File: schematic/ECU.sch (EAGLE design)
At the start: 29 parts, among them J1 Break, J2 COMM, J3 PWR, J4 DISPLAY, J5 THROTTLE, J6 LED, J7 SPEED, Q1 NMOSFETSOT23, Q2 NMOSFETSOT23, Q4 PMOSFET_BSS84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

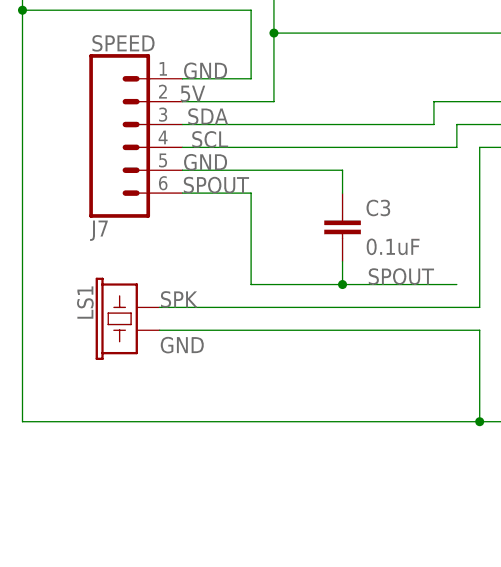
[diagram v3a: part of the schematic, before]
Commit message: Replace buzzer with 7.6mm contacts spacing
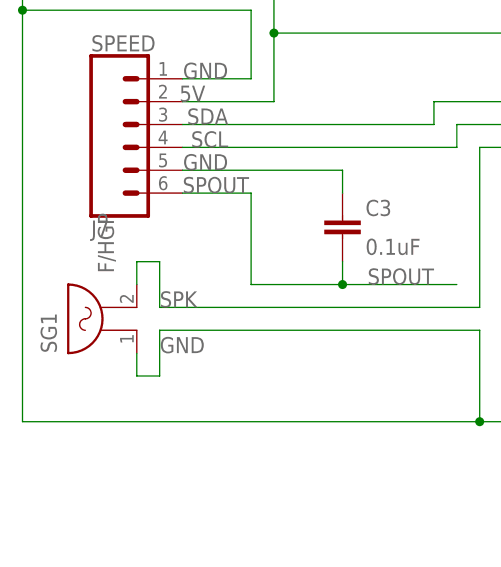
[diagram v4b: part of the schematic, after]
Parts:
- removed LS1: BUZZER-PTH_KIT, SparkFun-Electromechanical:BUZZER-PTH_KIT
- added SG1: F/HGP, buzzer:F/HGP
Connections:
- net GND: now also SG1.1; no longer LS1.2
- net SPK: now also SG1.2; no longer LS1.1
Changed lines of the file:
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@@
 <part name="C3" library="Capacitor" library_urn="urn:adsk.eagle:library:16290819" deviceset="C" device="CHIP-1206(3216-METRIC)" package3d_urn="urn:adsk.eagle:package:16290893/2" technology="_" value="0.1uF"/>
 <part name="Q1" library="Transistor" library_urn="urn:adsk.eagle:library:16378713" deviceset="NMOSFET" device="SOT23" package3d_urn="urn:adsk.eagle:package:28738/2"/>
-<part name="LS1" library="SparkFun-Electromechanical" library_urn="urn:adsk.eagle:library:516" deviceset="BUZZER" device="-PTH_KIT" package3d_urn="urn:adsk.eagle:package:38556/1"/>
 <part name="R3" library="eagle-ltspice" library_urn="urn:adsk.eagle:library:217" deviceset="R" device="R1206" package3d_urn="urn:adsk.eagle:package:13301/1" value="10K"/>
 <part name="D4" library="eScooter" deviceset="TVS_DIODE" device="SMA" package3d_urn="urn:adsk.eagle:package:21928182/1"/>
@@
 <part name="GND2" library="supply1" library_urn="urn:adsk.eagle:library:371" deviceset="GND" device=""/>
 <part name="U1" library="eScooter" deviceset="ARDUINO" device="ARDUINO_NANO" package3d_urn="urn:adsk.eagle:package:21849926/1" value="Arduino Nano Every"/>
+<part name="SG1" library="buzzer" library_urn="urn:adsk.eagle:library:113" deviceset="F/HGP" device="" package3d_urn="urn:adsk.eagle:package:5287/1"/>
 </parts>
 <sheets>
@@
 <attribute name="NAME" x="128.27" y="85.09" size="1.778" layer="95"/>
 </instance>
-<instance part="LS1" gate="G$1" x="-66.04" y="40.64" smashed="yes" rot="MR270">
-<attribute name="NAME" x="-70.866" y="43.18" size="1.778" layer="95" font="vector" rot="MR270"/>
-</instance>
 <instance part="R3" gate="G$1" x="134.62" y="33.02" smashed="yes" rot="R90">
 <attribute name="NAME" x="133.1214" y="29.21" size="1.778" layer="95" rot="R90"/>
@@
 <attribute name="NAME" x="27.94" y="86.36" size="1.778" layer="95"/>
 <attribute name="VALUE" x="20.32" y="40.64" size="1.778" layer="96"/>
+</instance>
+<instance part="SG1" gate="G$1" x="-68.58" y="38.1" smashed="yes" rot="R90">
+<attribute name="NAME" x="-74.93" y="35.56" size="1.778" layer="95" rot="R90"/>
+<attribute name="VALUE" x="-68.58" y="44.45" size="1.778" layer="96" rot="R90"/>
 </instance>
 </instances>
@@
 <label x="10.16" y="48.26" size="1.778" layer="95"/>
 <wire x1="0" y1="48.26" x2="0" y2="27.94" width="0.1524" layer="91"/>
-<pinref part="LS1" gate="G$1" pin="2"/>
 <wire x1="-63.5" y1="38.1" x2="-27.94" y2="38.1" width="0.1524" layer="91"/>
 <wire x1="-27.94" y1="38.1" x2="-27.94" y2="27.94" width="0.1524" layer="91"/>
@@
 <wire x1="66.04" y1="-17.78" x2="73.66" y2="-17.78" width="0.1524" layer="91"/>
 <pinref part="U1" gate="G$1" pin="GND"/>
+<pinref part="SG1" gate="G$1" pin="1"/>
+<wire x1="-66.04" y1="35.56" x2="-66.04" y2="33.02" width="0.1524" layer="91"/>
+<wire x1="-66.04" y1="33.02" x2="-63.5" y2="33.02" width="0.1524" layer="91"/>
+<wire x1="-63.5" y1="33.02" x2="-63.5" y2="38.1" width="0.1524" layer="91"/>
 </segment>
 <segment>
@@
 <wire x1="-27.94" y1="58.42" x2="-27.94" y2="40.64" width="0.1524" layer="91"/>
 <label x="10.16" y="58.42" size="1.778" layer="95"/>
-<pinref part="LS1" gate="G$1" pin="1"/>
 <wire x1="-63.5" y1="40.64" x2="-27.94" y2="40.64" width="0.1524" layer="91"/>
 <label x="-63.5" y="40.64" size="1.778" layer="95"/>
 <pinref part="U1" gate="G$1" pin="A6"/>
-</segment>
-</net>
+<pinref part="SG1" gate="G$1" pin="2"/>
+<wire x1="-66.04" y1="43.18" x2="-66.04" y2="45.72" width="0.1524" layer="91"/>
+<wire x1="-66.04" y1="45.72" x2="-63.5" y2="45.72" width="0.1524" layer="91"/>
+<wire x1="-63.5" y1="45.72" x2="-63.5" y2="40.64" width="0.1524" layer="91"/>
+</segment>
+</net>

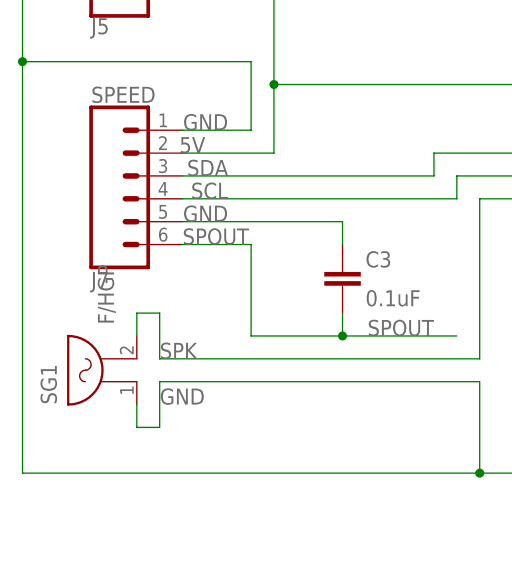
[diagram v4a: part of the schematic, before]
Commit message: Change MAX regulator package
- Change MAX package to drill-pin
- Move button to bottom layout
- Move elements for better work on regulator and ECU
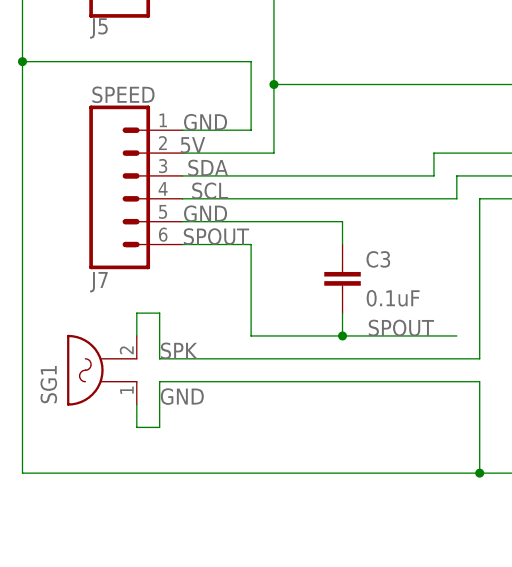
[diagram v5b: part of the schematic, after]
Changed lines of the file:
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@@
 <part name="Q4" library="Transistor" library_urn="urn:adsk.eagle:library:16378713" deviceset="PMOSFET_" device="" package3d_urn="urn:adsk.eagle:package:28738/2" technology="BSS84" value=""/>
 <part name="D3" library="Diode" library_urn="urn:adsk.eagle:library:16378169" deviceset="DIODE" device="DO-215-AC" package3d_urn="urn:adsk.eagle:package:9427057/2" technology="_" value=""/>
-<part name="S1" library="SparkFun-Switches" library_urn="urn:adsk.eagle:library:535" deviceset="MOMENTARY-SWITCH-SPST" device="-PTH-6.0MM" package3d_urn="urn:adsk.eagle:package:40163/1" value=""/>
 <part name="Q5" library="Transistor" library_urn="urn:adsk.eagle:library:16378713" deviceset="NMOSFET" device="SOT23" package3d_urn="urn:adsk.eagle:package:28738/2"/>
 <part name="J7" library="SparkFun-Connectors" library_urn="urn:adsk.eagle:library:513" deviceset="CONN_06" device="SILK_FEMALE_PTH" package3d_urn="urn:adsk.eagle:package:38009/1" value="SPEED"/>
@@
 <part name="GND2" library="supply1" library_urn="urn:adsk.eagle:library:371" deviceset="GND" device=""/>
 <part name="U1" library="eScooter" deviceset="ARDUINO" device="ARDUINO_NANO" package3d_urn="urn:adsk.eagle:package:21849926/1" value="Arduino Nano Every"/>
-<part name="SG1" library="buzzer" library_urn="urn:adsk.eagle:library:113" deviceset="F/HGP" device="" package3d_urn="urn:adsk.eagle:package:5287/1"/>
+<part name="S1" library="SparkFun-Switches" deviceset="MOMENTARY-SWITCH-SPST" device="-PTH-6.0MM" package3d_urn="urn:adsk.eagle:package:40163/1"/>
+<part name="SG1" library="buzzer" deviceset="F/HGP" device="" package3d_urn="urn:adsk.eagle:package:5287/1"/>
 </parts>
 <sheets>
@@
 <attribute name="VALUE" x="81.28" y="-33.02" size="1.778" layer="95" align="center"/>
 </instance>
-<instance part="S1" gate="G$1" x="88.9" y="-10.16" smashed="yes">
-<attribute name="NAME" x="88.9" y="-8.636" size="1.778" layer="95" font="vector" align="bottom-center"/>
-<attribute name="VALUE" x="88.9" y="-10.668" size="1.778" layer="96" font="vector" align="top-center"/>
-</instance>
 <instance part="Q5" gate="G$1" x="88.9" y="50.8" smashed="yes" rot="MR0">
 <attribute name="NAME" x="82.55" y="52.07" size="1.778" layer="95" rot="MR0"/>
@@
 <attribute name="VALUE" x="20.32" y="40.64" size="1.778" layer="96"/>
 </instance>
+<instance part="S1" gate="G$1" x="88.9" y="-10.16" smashed="yes">
+<attribute name="NAME" x="88.9" y="-8.636" size="1.778" layer="95" font="vector" align="bottom-center"/>
+</instance>
 <instance part="SG1" gate="G$1" x="-68.58" y="38.1" smashed="yes" rot="R90">
 <attribute name="NAME" x="-74.93" y="35.56" size="1.778" layer="95" rot="R90"/>
-<attribute name="VALUE" x="-68.58" y="44.45" size="1.778" layer="96" rot="R90"/>
 </instance>
 </instances>
@@
 <wire x1="88.9" y1="-5.08" x2="88.9" y2="0" width="0.1524" layer="91"/>
 <label x="55.88" y="-10.16" size="1.778" layer="95"/>
-<pinref part="S1" gate="G$1" pin="1"/>
 <wire x1="88.9" y1="0" x2="88.9" y2="2.54" width="0.1524" layer="91"/>
 <wire x1="83.82" y1="-10.16" x2="76.2" y2="-10.16" width="0.1524" layer="91"/>
@@
 <wire x1="66.04" y1="-17.78" x2="73.66" y2="-17.78" width="0.1524" layer="91"/>
 <pinref part="U1" gate="G$1" pin="GND"/>
-<pinref part="SG1" gate="G$1" pin="1"/>
 <wire x1="-66.04" y1="35.56" x2="-66.04" y2="33.02" width="0.1524" layer="91"/>
 <wire x1="-66.04" y1="33.02" x2="-63.5" y2="33.02" width="0.1524" layer="91"/>
 <wire x1="-63.5" y1="33.02" x2="-63.5" y2="38.1" width="0.1524" layer="91"/>
+<pinref part="S1" gate="G$1" pin="1"/>
+<pinref part="SG1" gate="G$1" pin="1"/>
 </segment>
 <segment>
@@
 <wire x1="86.36" y1="-27.94" x2="99.06" y2="-27.94" width="0.1524" layer="91"/>
 <wire x1="99.06" y1="-10.16" x2="99.06" y2="-7.62" width="0.1524" layer="91"/>
-<pinref part="S1" gate="G$1" pin="2"/>
 <wire x1="99.06" y1="-17.78" x2="99.06" y2="-27.94" width="0.1524" layer="91"/>
 <wire x1="99.06" y1="-17.78" x2="88.9" y2="-17.78" width="0.1524" layer="91"/>
@@
 <wire x1="99.06" y1="-10.16" x2="99.06" y2="-17.78" width="0.1524" layer="91"/>
 <junction x="99.06" y="-10.16"/>
+<pinref part="S1" gate="G$1" pin="2"/>
 </segment>
 </net>
@@
 <label x="-63.5" y="40.64" size="1.778" layer="95"/>
 <pinref part="U1" gate="G$1" pin="A6"/>
-<pinref part="SG1" gate="G$1" pin="2"/>
 <wire x1="-66.04" y1="43.18" x2="-66.04" y2="45.72" width="0.1524" layer="91"/>
 <wire x1="-66.04" y1="45.72" x2="-63.5" y2="45.72" width="0.1524" layer="91"/>
 <wire x1="-63.5" y1="45.72" x2="-63.5" y2="40.64" width="0.1524" layer="91"/>
-</segment>
-</net>
+<pinref part="SG1" gate="G$1" pin="2"/>
+</segment>
+</net>

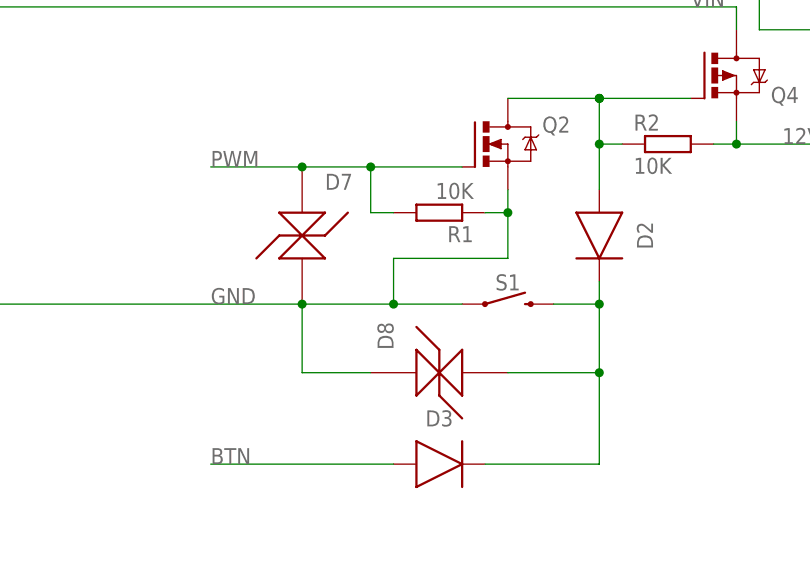
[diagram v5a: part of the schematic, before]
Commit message: Rework ECU board
- Align sizes
- Align elements placement on layers
- Change power traces in regulator
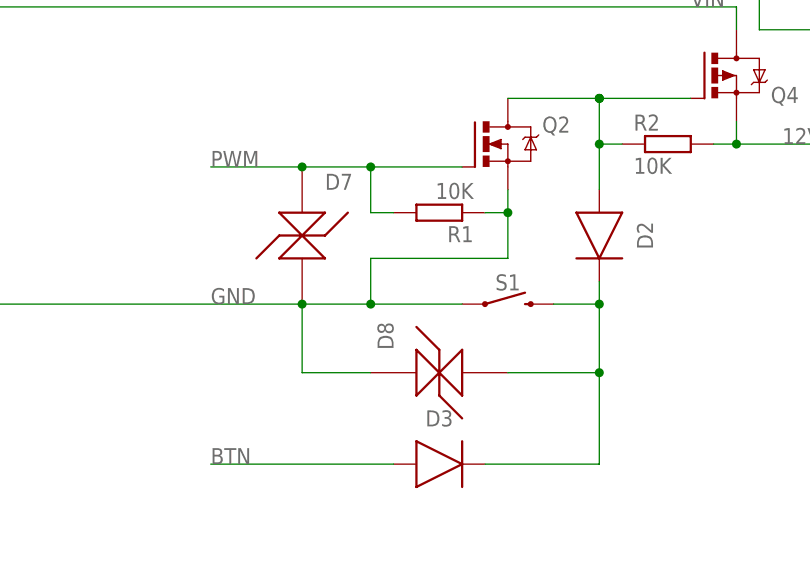
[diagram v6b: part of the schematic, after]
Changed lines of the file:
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@@
 <pinref part="R1" gate="G$1" pin="1"/>
 <pinref part="Q2" gate="G$1" pin="S"/>
-<wire x1="76.2" y1="-5.08" x2="88.9" y2="-5.08" width="0.1524" layer="91"/>
+<wire x1="73.66" y1="-5.08" x2="88.9" y2="-5.08" width="0.1524" layer="91"/>
 <wire x1="88.9" y1="-5.08" x2="88.9" y2="0" width="0.1524" layer="91"/>
 <label x="55.88" y="-10.16" size="1.778" layer="95"/>
 <wire x1="88.9" y1="0" x2="88.9" y2="2.54" width="0.1524" layer="91"/>
-<wire x1="83.82" y1="-10.16" x2="76.2" y2="-10.16" width="0.1524" layer="91"/>
-<wire x1="76.2" y1="-5.08" x2="76.2" y2="-10.16" width="0.1524" layer="91"/>
-<junction x="76.2" y="-10.16"/>
-<wire x1="76.2" y1="-10.16" x2="66.04" y2="-10.16" width="0.1524" layer="91"/>
+<wire x1="83.82" y1="-10.16" x2="73.66" y2="-10.16" width="0.1524" layer="91"/>
+<wire x1="73.66" y1="-5.08" x2="73.66" y2="-10.16" width="0.1524" layer="91"/>
+<junction x="73.66" y="-10.16"/>
+<wire x1="73.66" y1="-10.16" x2="66.04" y2="-10.16" width="0.1524" layer="91"/>
 <wire x1="86.36" y1="0" x2="88.9" y2="0" width="0.1524" layer="91"/>
 <junction x="88.9" y="0"/>

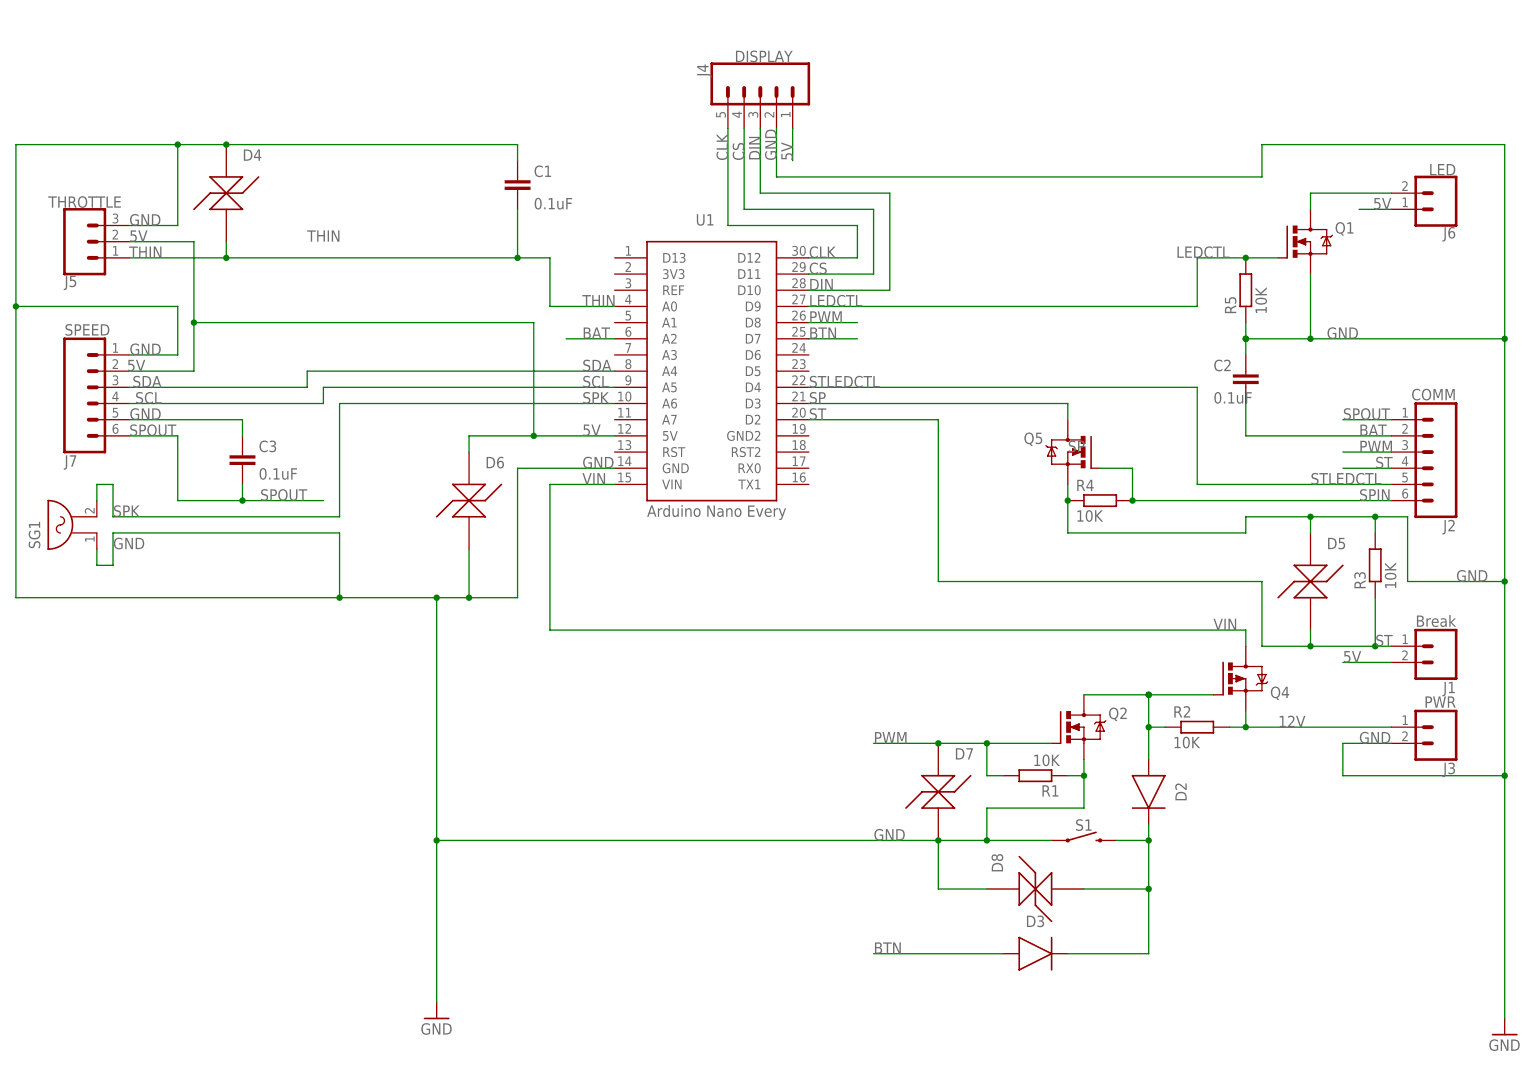
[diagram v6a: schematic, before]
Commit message: Remove high-side switch for driver
- Keep driver alway on for now
- Add mosfet switched for speed and throttle
- Align break work
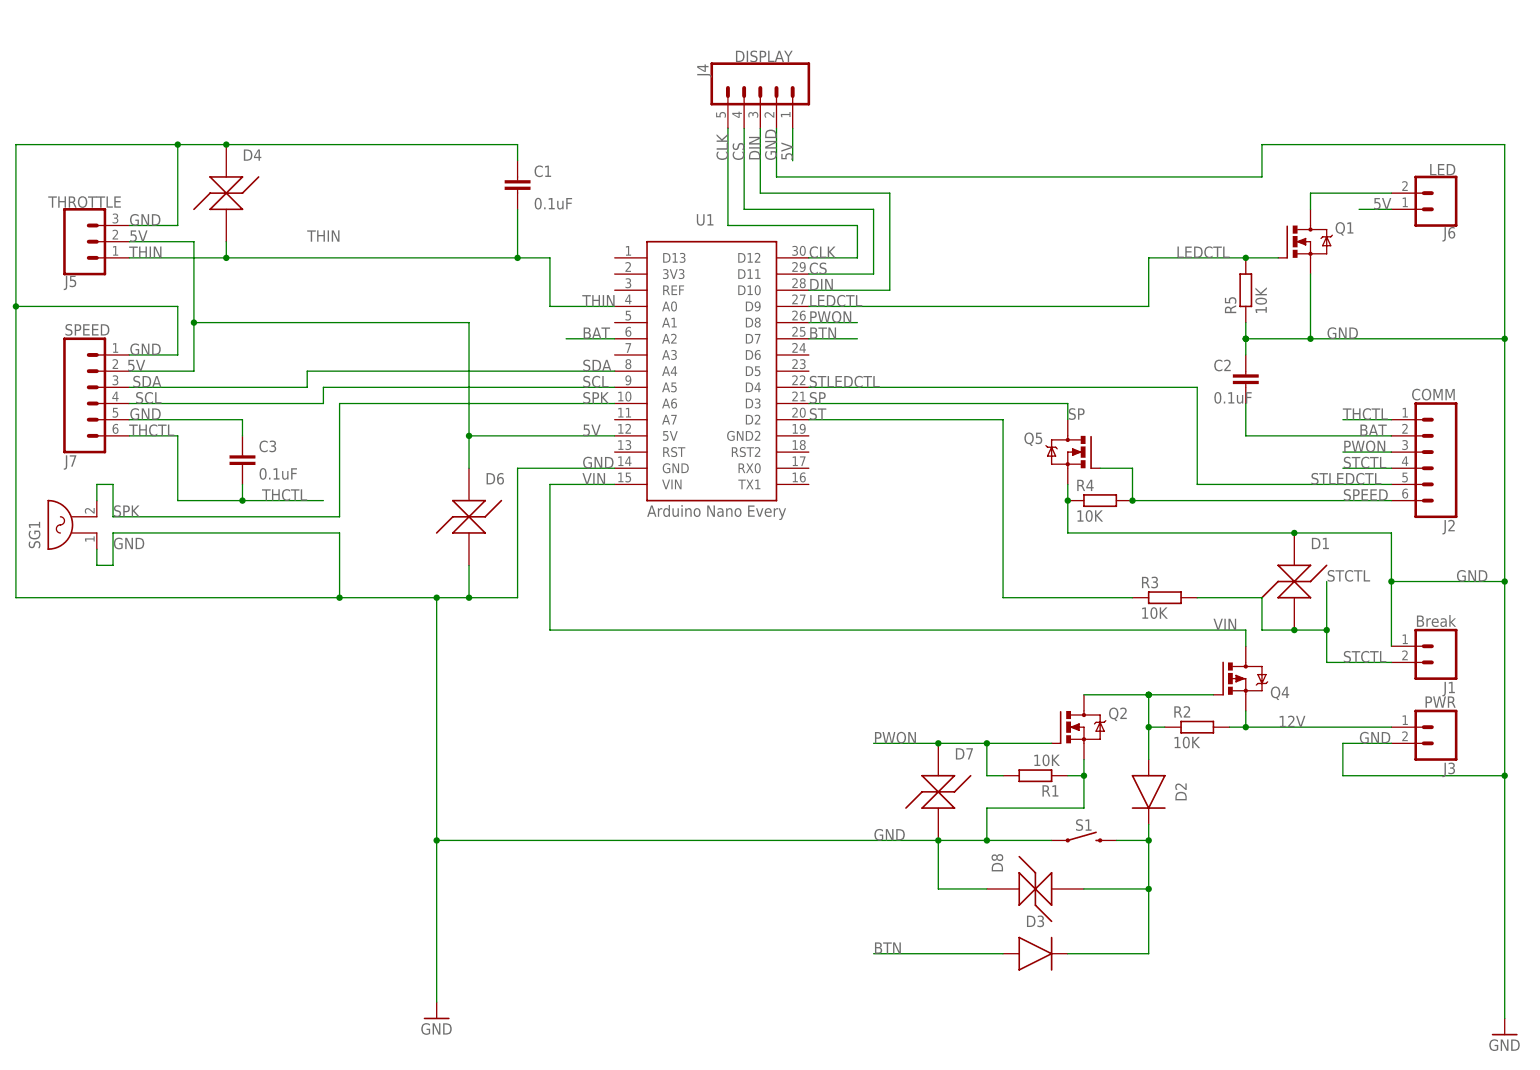
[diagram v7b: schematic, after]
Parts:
- removed D5: TVS_DIODESMA, eScooter:TVS_DIODESMA
- added D1: TVS_DIODESMA, eScooter:TVS_DIODESMA
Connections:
- net PWM renamed PWON
- net SPIN renamed SPEED
- net SPOUT renamed THCTL
- new net STCTL: D1.P$2, J1.2, J2.4, R3.2
- net 5V: no longer J1.2
- net GND: now also D1.P$1, J1.1; no longer D5.P$1, R3.2
- net ST: no longer D5.P$2, J1.1, J2.4
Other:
- moved on the sheet: D6, R3
